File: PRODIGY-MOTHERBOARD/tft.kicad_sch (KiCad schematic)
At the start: 1 part, among them U11 CR2013-MI2120

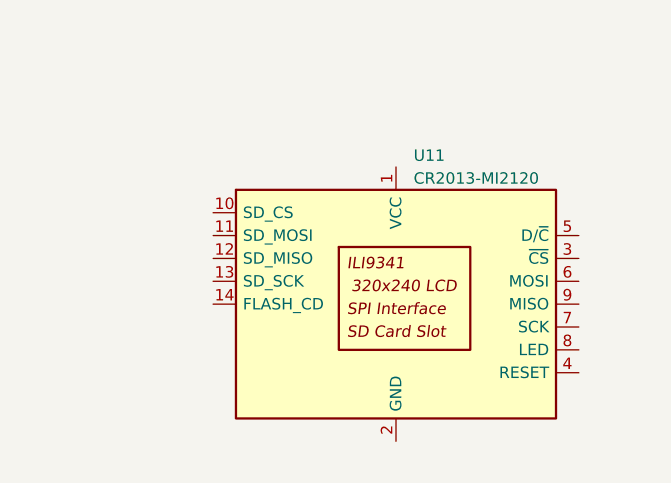
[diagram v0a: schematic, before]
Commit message: Finished neopixel and button's schematic.
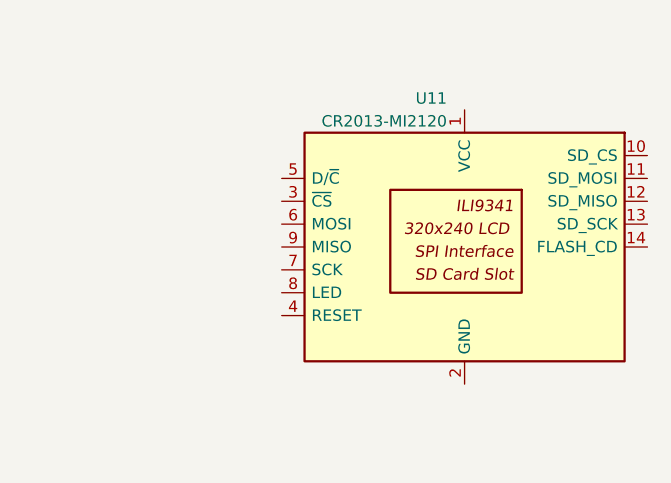
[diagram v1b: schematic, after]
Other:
- moved on the sheet: U11
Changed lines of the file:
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@@
 	(symbol
 		(lib_id "Driver_Display:CR2013-MI2120")
-		(at 134.62 93.98 0)
+		(at 142.24 87.63 0)
+		(mirror y)
 		(unit 1)
 		(exclude_from_sim no)
@@
 		(on_board yes)
 		(dnp no)
-		(fields_autoplaced yes)
 		(property "Reference" "U11"
-			(at 136.5759 77.47 0)
+			(at 140.2841 71.12 0)
 			(effects
 				(font
@@
 		)
 		(property "Value" "CR2013-MI2120"
-			(at 136.5759 80.01 0)
+			(at 140.2841 73.66 0)
 			(effects
 				(font
@@
 		)
 		(property "Footprint" "Display:CR2013-MI2120"
-			(at 134.62 111.76 0)
+			(at 142.24 105.41 0)
 			(effects
 				(font
@@
 		)
 		(property "Datasheet" "http://pan.baidu.com/s/11Y990"
-			(at 118.11 81.28 0)
+			(at 158.75 74.93 0)
 			(effects
 				(font
@@
 		)
 		(property "Description" ""
-			(at 134.62 93.98 0)
+			(at 142.24 87.63 0)
 			(effects
 				(font

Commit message: CAN schematic done
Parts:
- renumbered U11 to U16
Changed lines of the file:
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@@
 		(on_board yes)
 		(dnp no)
-		(property "Reference" "U11"
+		(property "Reference" "U16"
 			(at 140.2841 71.12 0)
 			(effects
@@
 			(project "PRODIGY-MOTHERBOARD"
 				(path "/f1c25860-8989-4190-bd24-2491d23ca7d9/e2913798-f444-47a6-8b64-53020d7d816b/1de6bd67-9d33-41f3-aec8-5ac609c7db7f"
-					(reference "U11")
+					(reference "U16")
 					(unit 1)
 				)

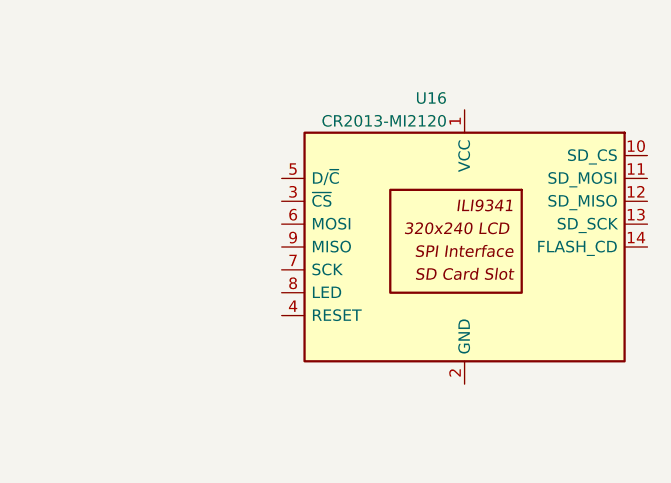
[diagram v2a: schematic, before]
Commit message: Added pins to MCU. Added Decoder for SPI SS-Multiplexing.
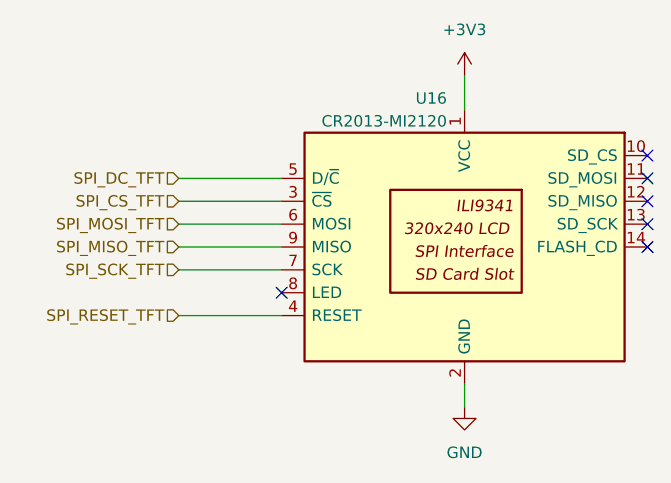
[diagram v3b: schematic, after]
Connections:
- net +3V3: now reaches U16.1 (VCC)
- net GND: now reaches U16.2 (GND)
- net SPI_CS_TFT: now reaches U16.3 (~{CS})
- net SPI_RESET_TFT: now reaches U16.4 (RESET)
- net SPI_DC_TFT: now reaches U16.5 (D/~{C})
- net SPI_MOSI_TFT: now reaches U16.6 (MOSI)
- net SPI_SCK_TFT: now reaches U16.7 (SCK)
- net SPI_MISO_TFT: now reaches U16.9 (MISO)
- no-connect marks 0 -> 6

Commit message: Added proper debounce filter elements to buttons.
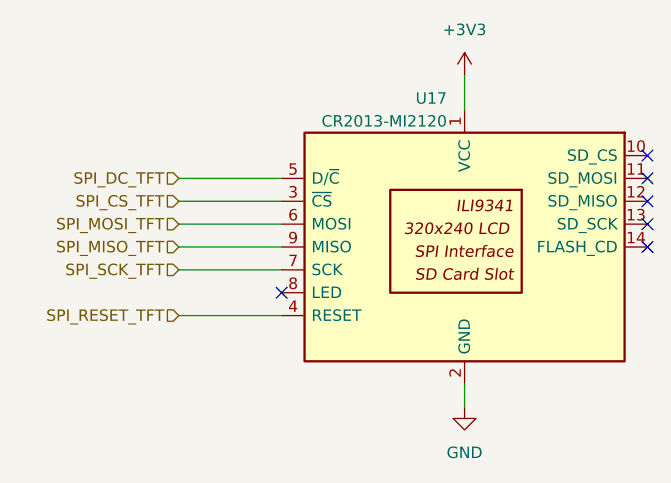
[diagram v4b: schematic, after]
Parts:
- renumbered U16 to U17
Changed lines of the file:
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@@
 		(on_board yes)
 		(dnp no)
-		(property "Reference" "U16"
+		(property "Reference" "U17"
 			(at 140.2841 71.12 0)
 			(effects
@@
 			(project "PRODIGY-MOTHERBOARD"
 				(path "/f1c25860-8989-4190-bd24-2491d23ca7d9/e2913798-f444-47a6-8b64-53020d7d816b/1de6bd67-9d33-41f3-aec8-5ac609c7db7f"
-					(reference "U16")
+					(reference "U17")
 					(unit 1)
 				)
@@
 		(dnp no)
 		(fields_autoplaced yes)
-		(property "Reference" "#PWR0191"
+		(property "Reference" "#PWR099"
 			(at 142.24 111.76 0)
 			(effects
@@
 			(project "PRODIGY-MOTHERBOARD"
 				(path "/f1c25860-8989-4190-bd24-2491d23ca7d9/e2913798-f444-47a6-8b64-53020d7d816b/1de6bd67-9d33-41f3-aec8-5ac609c7db7f"
-					(reference "#PWR0191")
+					(reference "#PWR099")
 					(unit 1)
 				)
@@
 		(dnp no)
 		(fields_autoplaced yes)
-		(property "Reference" "#PWR0190"
+		(property "Reference" "#PWR098"
 			(at 142.24 72.39 0)
 			(effects
@@
 			(project "PRODIGY-MOTHERBOARD"
 				(path "/f1c25860-8989-4190-bd24-2491d23ca7d9/e2913798-f444-47a6-8b64-53020d7d816b/1de6bd67-9d33-41f3-aec8-5ac609c7db7f"
-					(reference "#PWR0190")
+					(reference "#PWR098")
 					(unit 1)
 				)

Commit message: Submitted V0 for evaluation. Avaiting feedback.
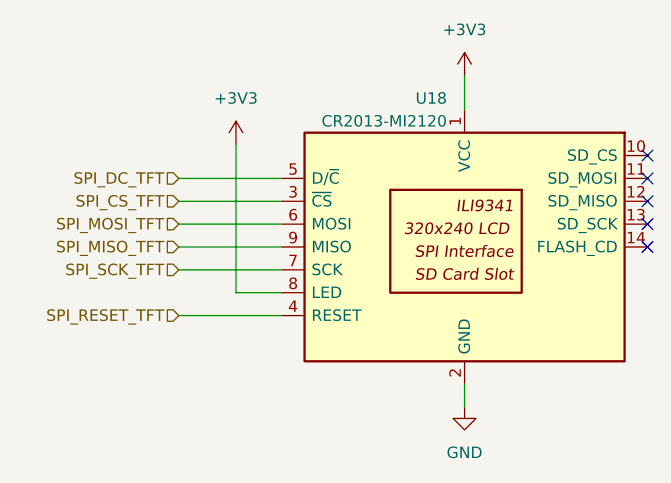
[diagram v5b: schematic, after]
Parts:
- renumbered U17 to U18
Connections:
- net +3V3: now also U18.8 (LED)
- no-connect marks 6 -> 5
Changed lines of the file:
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@@
 	(paper "A4")
 	(no_connect
-		(at 121.92 92.71)
-	)
-	(no_connect
 		(at 162.56 80.01)
 	)
@@
 	(wire
 		(pts
+			(xy 121.92 92.71) (xy 116.84 92.71)
+		)
+		(stroke
+			(width 0)
+			(type default)
+		)
+	)
+	(wire
+		(pts
 			(xy 110.49 82.55) (xy 121.92 82.55)
+		)
+		(stroke
+			(width 0)
+			(type default)
+		)
+	)
+	(wire
+		(pts
+			(xy 116.84 76.2) (xy 116.84 92.71)
 		)
 		(stroke
@@
 		(on_board yes)
 		(dnp no)
-		(property "Reference" "U17"
+		(property "Reference" "U18"
 			(at 140.2841 71.12 0)
 			(effects
@@
 			(project "PRODIGY-MOTHERBOARD"
 				(path "/f1c25860-8989-4190-bd24-2491d23ca7d9/e2913798-f444-47a6-8b64-53020d7d816b/1de6bd67-9d33-41f3-aec8-5ac609c7db7f"
-					(reference "U17")
+					(reference "U18")
 					(unit 1)
 				)
@@
 		(dnp no)
 		(fields_autoplaced yes)
-		(property "Reference" "#PWR099"
+		(property "Reference" "#PWR0129"
 			(at 142.24 111.76 0)
 			(effects
@@
 			(project "PRODIGY-MOTHERBOARD"
 				(path "/f1c25860-8989-4190-bd24-2491d23ca7d9/e2913798-f444-47a6-8b64-53020d7d816b/1de6bd67-9d33-41f3-aec8-5ac609c7db7f"
-					(reference "#PWR099")
+					(reference "#PWR0129")
 					(unit 1)
 				)
@@
 		(dnp no)
 		(fields_autoplaced yes)
-		(property "Reference" "#PWR098"
+		(property "Reference" "#PWR0127"
 			(at 142.24 72.39 0)
 			(effects
@@
 			(project "PRODIGY-MOTHERBOARD"
 				(path "/f1c25860-8989-4190-bd24-2491d23ca7d9/e2913798-f444-47a6-8b64-53020d7d816b/1de6bd67-9d33-41f3-aec8-5ac609c7db7f"
-					(reference "#PWR098")
+					(reference "#PWR0127")
 					(unit 1)
 				)
+			)
+		)
+	)
+	(symbol
+		(lib_id "power:+3V3")
+		(at 116.84 76.2 0)
+		(unit 1)
+		(exclude_from_sim no)
+		(in_bom yes)
+		(on_board yes)
+		(dnp no)
+		(fields_autoplaced yes)
+		(property "Reference" "#PWR0128"
+			(at 116.84 80.01 0)
+			(effects
+				(font
+					(size 1.27 1.27)
+				)
+				(hide yes)
+			)
+		)
+		(property "Value" "+3V3"
+			(at 116.84 71.12 0)
+			(effects
+				(font
+					(size 1.27 1.27)
+				)
+			)
+		)
+		(property "Footprint" ""
+			(at 116.84 76.2 0)
+			(effects
+				(font
+					(size 1.27 1.27)
+				)
+				(hide yes)
+			)
+		)
+		(property "Datasheet" ""
+			(at 116.84 76.2 0)
+			(effects
+				(font
+					(size 1.27 1.27)
+				)
+				(hide yes)
+			)
+		)
+		(property "Description" "Power symbol creates a global label with name \"+3V3\""
+			(at 116.84 76.2 0)
+			(effects
+				(font
+					(size 1.27 1.27)
+				)
+				(hide yes)
+			)
+		)
+		(pin "1"
+		)
+		(instances
+			(project "PRODIGY-MOTHERBOARD"
+				(path "/f1c25860-8989-4190-bd24-2491d23ca7d9/e2913798-f444-47a6-8b64-53020d7d816b/1de6bd67-9d33-41f3-aec8-5ac609c7db7f"
+					(reference "#PWR0128")
+					(unit 1)
+				)

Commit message: schematic v0.2 finalized
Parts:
- renumbered U18 to U17
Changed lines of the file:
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@@
 		(on_board yes)
 		(dnp no)
-		(property "Reference" "U18"
+		(property "Reference" "U17"
 			(at 140.2841 71.12 0)
 			(effects
@@
 			(project "PRODIGY-MOTHERBOARD"
 				(path "/f1c25860-8989-4190-bd24-2491d23ca7d9/e2913798-f444-47a6-8b64-53020d7d816b/1de6bd67-9d33-41f3-aec8-5ac609c7db7f"
-					(reference "U18")
+					(reference "U17")
 					(unit 1)
 				)
@@
 		(dnp no)
 		(fields_autoplaced yes)
-		(property "Reference" "#PWR0168"
+		(property "Reference" "#PWR0166"
 			(at 142.24 111.76 0)
 			(effects
@@
 			(project "PRODIGY-MOTHERBOARD"
 				(path "/f1c25860-8989-4190-bd24-2491d23ca7d9/e2913798-f444-47a6-8b64-53020d7d816b/1de6bd67-9d33-41f3-aec8-5ac609c7db7f"
-					(reference "#PWR0168")
+					(reference "#PWR0166")
 					(unit 1)
 				)
@@
 		(dnp no)
 		(fields_autoplaced yes)
-		(property "Reference" "#PWR0167"
+		(property "Reference" "#PWR0165"
 			(at 142.24 72.39 0)
 			(effects
@@
 			(project "PRODIGY-MOTHERBOARD"
 				(path "/f1c25860-8989-4190-bd24-2491d23ca7d9/e2913798-f444-47a6-8b64-53020d7d816b/1de6bd67-9d33-41f3-aec8-5ac609c7db7f"
-					(reference "#PWR0167")
+					(reference "#PWR0165")
 					(unit 1)
 				)
@@
 		(dnp no)
 		(fields_autoplaced yes)
-		(property "Reference" "#PWR0166"
+		(property "Reference" "#PWR0164"
 			(at 116.84 80.01 0)
 			(effects
@@
 			(project "PRODIGY-MOTHERBOARD"
 				(path "/f1c25860-8989-4190-bd24-2491d23ca7d9/e2913798-f444-47a6-8b64-53020d7d816b/1de6bd67-9d33-41f3-aec8-5ac609c7db7f"
-					(reference "#PWR0166")
-					(unit 1)
-				)
+					(reference "#PWR0164")
+					(unit 1)
+				)

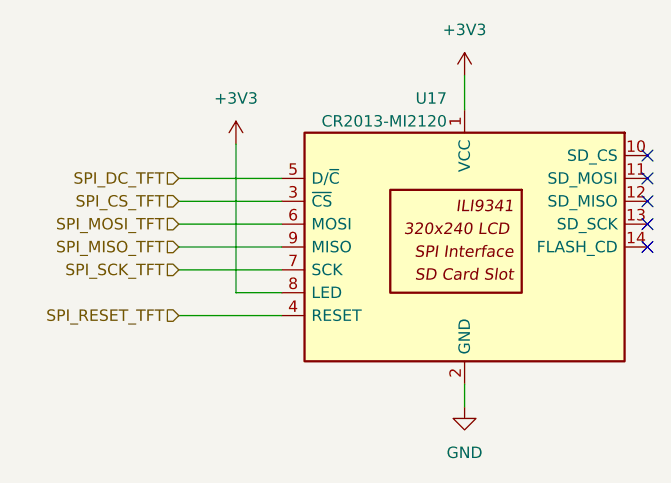
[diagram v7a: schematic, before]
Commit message: Motherboard footprints assigned.
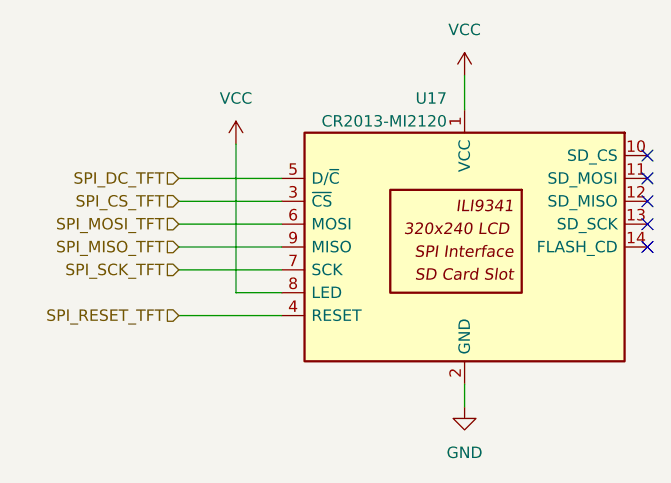
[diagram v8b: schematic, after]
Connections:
- net +3V3 renamed VCC
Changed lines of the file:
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@@
+	)
+	(symbol
+		(lib_id "power:VCC")
+		(at 142.24 68.58 0)
+		(unit 1)
+		(exclude_from_sim no)
+		(in_bom yes)
+		(on_board yes)
+		(dnp no)
+		(fields_autoplaced yes)
+		(property "Reference" "#PWR0165"
+			(at 142.24 72.39 0)
+			(effects
+				(font
+					(size 1.27 1.27)
+				)
+				(hide yes)
+			)
+		)
+		(property "Value" "VCC"
+			(at 142.24 63.5 0)
+			(effects
+				(font
+					(size 1.27 1.27)
+				)
+			)
+		)
+		(property "Footprint" ""
+			(at 142.24 68.58 0)
+			(effects
+				(font
+					(size 1.27 1.27)
+				)
+				(hide yes)
+			)
+		)
+		(property "Datasheet" ""
+			(at 142.24 68.58 0)
+			(effects
+				(font
+					(size 1.27 1.27)
+				)
+				(hide yes)
+			)
+		)
+		(property "Description" "Power symbol creates a global label with name \"VCC\""
+			(at 142.24 68.58 0)
+			(effects
+				(font
+					(size 1.27 1.27)
+				)
+				(hide yes)
+			)
+		)
+		(pin "1"
+		)
+		(instances
+			(project "PRODIGY-MOTHERBOARD"
+				(path "/f1c25860-8989-4190-bd24-2491d23ca7d9/e2913798-f444-47a6-8b64-53020d7d816b/1de6bd67-9d33-41f3-aec8-5ac609c7db7f"
+					(reference "#PWR0165")
+					(unit 1)
+				)
+			)
+		)
+	)
+	(symbol
+		(lib_id "power:VCC")
+		(at 116.84 76.2 0)
+		(unit 1)
+		(exclude_from_sim no)
+		(in_bom yes)
+		(on_board yes)
+		(dnp no)
+		(fields_autoplaced yes)
+		(property "Reference" "#PWR0164"
+			(at 116.84 80.01 0)
+			(effects
+				(font
+					(size 1.27 1.27)
+				)
+				(hide yes)
+			)
+		)
+		(property "Value" "VCC"
+			(at 116.84 71.12 0)
+			(effects
+				(font
+					(size 1.27 1.27)
+				)
+			)
+		)
+		(property "Footprint" ""
+			(at 116.84 76.2 0)
+			(effects
+				(font
+					(size 1.27 1.27)
+				)
+				(hide yes)
+			)
+		)
+		(property "Datasheet" ""
+			(at 116.84 76.2 0)
+			(effects
+				(font
+					(size 1.27 1.27)
+				)
+				(hide yes)
+			)
+		)
+		(property "Description" "Power symbol creates a global label with name \"VCC\""
+			(at 116.84 76.2 0)
+			(effects
+				(font
+					(size 1.27 1.27)
+				)
+				(hide yes)
+			)
+		)
+		(pin "1"
+		)
+		(instances
+			(project "PRODIGY-MOTHERBOARD"
+				(path "/f1c25860-8989-4190-bd24-2491d23ca7d9/e2913798-f444-47a6-8b64-53020d7d816b/1de6bd67-9d33-41f3-aec8-5ac609c7db7f"
+					(reference "#PWR0164")
+					(unit 1)
+				)
+			)
+		)
 	)
 	(symbol
@@
 			)
 		)
+		(property "MOUSER" ""
+			(at 142.24 87.63 0)
+			(effects
+				(font
+					(size 1.27 1.27)
+				)
+				(hide yes)
+			)
+		)
+		(property "Sim.Type" ""
+			(at 142.24 87.63 0)
+			(effects
+				(font
+					(size 1.27 1.27)
+				)
+				(hide yes)
+			)
+		)
+		(property "TME" ""
+			(at 142.24 87.63 0)
+			(effects
+				(font
+					(size 1.27 1.27)
+				)
+				(hide yes)
+			)
+		)
 		(pin "1"
 		)
@@
 					(unit 1)
 				)
-			)
-		)
-	)
-	(symbol
-		(lib_id "power:+3V3")
-		(at 142.24 68.58 0)
-		(unit 1)
-		(exclude_from_sim no)
-		(in_bom yes)
-		(on_board yes)
-		(dnp no)
-		(fields_autoplaced yes)
-		(property "Reference" "#PWR0165"
-			(at 142.24 72.39 0)
-			(effects
-				(font
-					(size 1.27 1.27)
-				)
-				(hide yes)
-			)
-		)
-		(property "Value" "+3V3"
-			(at 142.24 63.5 0)
-			(effects
-				(font
-					(size 1.27 1.27)
-				)
-			)
-		)
-		(property "Footprint" ""
-			(at 142.24 68.58 0)
-			(effects
-				(font
-					(size 1.27 1.27)
-				)
-				(hide yes)
-			)
-		)
-		(property "Datasheet" ""
-			(at 142.24 68.58 0)
-			(effects
-				(font
-					(size 1.27 1.27)
-				)
-				(hide yes)
-			)
-		)
-		(property "Description" "Power symbol creates a global label with name \"+3V3\""
-			(at 142.24 68.58 0)
-			(effects
-				(font
-					(size 1.27 1.27)
-				)
-				(hide yes)
-			)
-		)
-		(pin "1"
-		)
-		(instances
-			(project "PRODIGY-MOTHERBOARD"
-				(path "/f1c25860-8989-4190-bd24-2491d23ca7d9/e2913798-f444-47a6-8b64-53020d7d816b/1de6bd67-9d33-41f3-aec8-5ac609c7db7f"
-					(reference "#PWR0165")
-					(unit 1)
-				)
-			)
-		)
-	)
-	(symbol
-		(lib_id "power:+3V3")
-		(at 116.84 76.2 0)
-		(unit 1)
-		(exclude_from_sim no)
-		(in_bom yes)
-		(on_board yes)
-		(dnp no)
-		(fields_autoplaced yes)
-		(property "Reference" "#PWR0164"
-			(at 116.84 80.01 0)
-			(effects
-				(font
-					(size 1.27 1.27)
-				)
-				(hide yes)
-			)
-		)
-		(property "Value" "+3V3"
-			(at 116.84 71.12 0)
-			(effects
-				(font
-					(size 1.27 1.27)
-				)
-			)
-		)
-		(property "Footprint" ""
-			(at 116.84 76.2 0)
-			(effects
-				(font
-					(size 1.27 1.27)
-				)
-				(hide yes)
-			)
-		)
-		(property "Datasheet" ""
-			(at 116.84 76.2 0)
-			(effects
-				(font
-					(size 1.27 1.27)
-				)
-				(hide yes)
-			)
-		)
-		(property "Description" "Power symbol creates a global label with name \"+3V3\""
-			(at 116.84 76.2 0)
-			(effects
-				(font
-					(size 1.27 1.27)
-				)
-				(hide yes)
-			)
-		)
-		(pin "1"
-		)
-		(instances
-			(project "PRODIGY-MOTHERBOARD"
-				(path "/f1c25860-8989-4190-bd24-2491d23ca7d9/e2913798-f444-47a6-8b64-53020d7d816b/1de6bd67-9d33-41f3-aec8-5ac609c7db7f"
-					(reference "#PWR0164")
-					(unit 1)
-				)
